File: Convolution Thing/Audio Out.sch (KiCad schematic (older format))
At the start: 25 parts, among them J4 Out Left, J5 Out Right, U4 NE5532

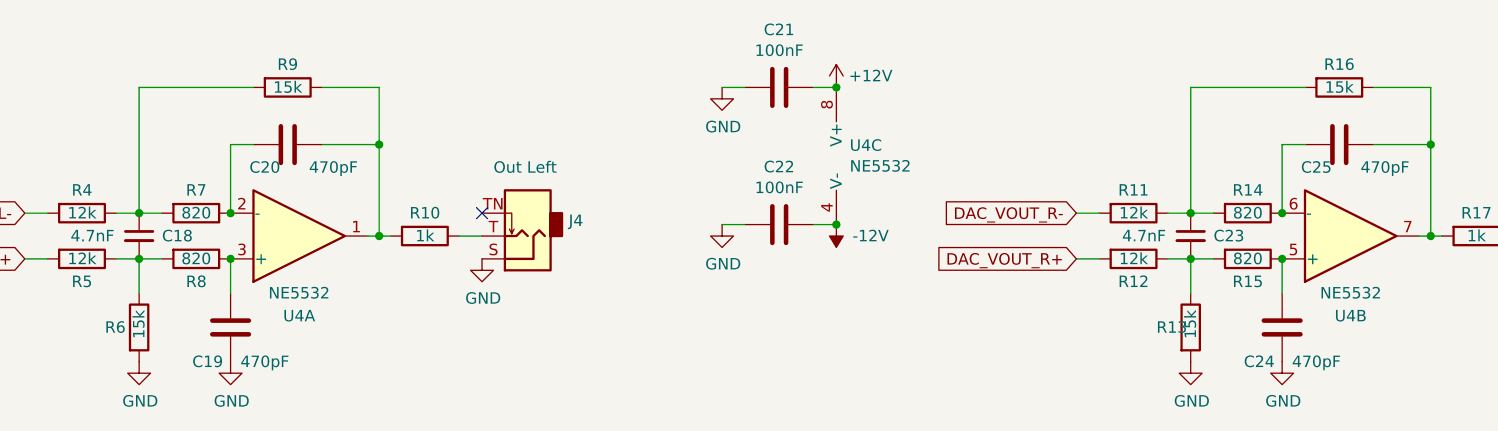
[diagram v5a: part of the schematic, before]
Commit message: Assign all footprints
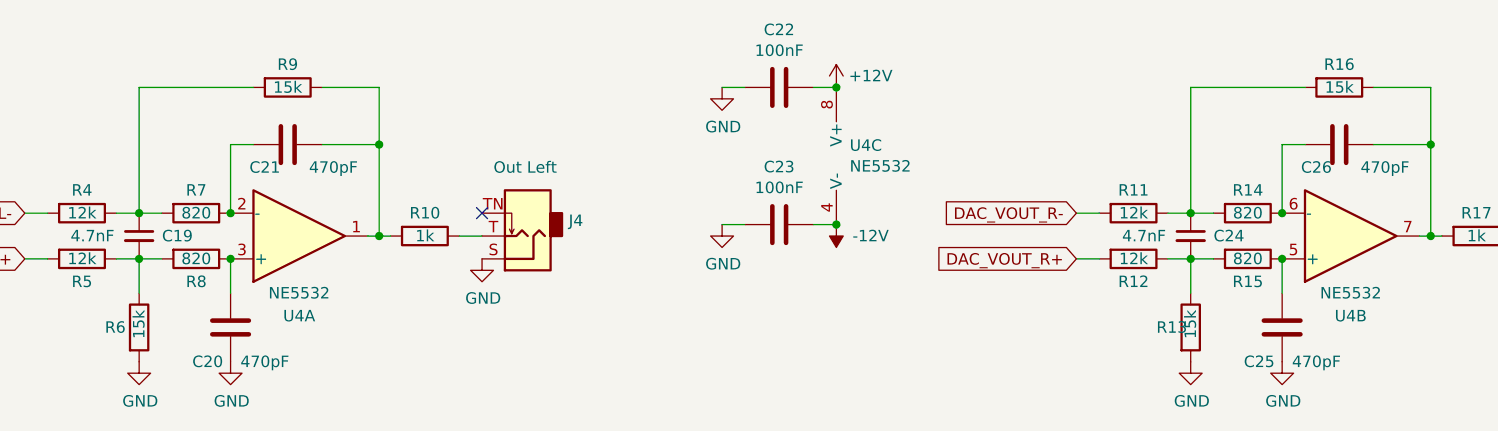
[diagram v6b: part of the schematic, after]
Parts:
- C19: renamed from C18; footprint (none) -> Capacitor_SMD:C_0805_2012Metric
- C20: renamed from C19; footprint (none) -> Capacitor_SMD:C_0805_2012Metric
- C21: renamed from C20; footprint (none) -> Capacitor_SMD:C_0805_2012Metric
- C22: renamed from C21; footprint (none) -> Capacitor_SMD:C_0805_2012Metric
- C23: renamed from C22; footprint (none) -> Capacitor_SMD:C_0805_2012Metric
- C24: renamed from C23; footprint (none) -> Capacitor_SMD:C_0805_2012Metric
- C25: renamed from C24; footprint (none) -> Capacitor_SMD:C_0805_2012Metric
- C26: renamed from C25; footprint (none) -> Capacitor_SMD:C_0805_2012Metric
- J4, J5: footprint (none) -> SamacSys:ACJMNV352S
- R10, R11, R12, R13, R14, R15, R16, R17, R4, R5, R6, R7, R8, R9: footprint (none) -> Resistor_SMD:R_0805_2012Metric
- U4: footprint (none) -> Package_SO:SOIC-8_3.9x4.9mm_P1.27mm
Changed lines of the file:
@@
 F 0 "U4" H 2350 2000 50  0000 C CNN
 F 1 "NE5532" H 2350 1900 50  0000 C CNN
-F 2 "" H 2350 1650 50  0001 C CNN
+F 2 "Package_SO:SOIC-8_3.9x4.9mm_P1.27mm" H 2350 1650 50  0001 C CNN
 F 3 "http://www.ti.com/lit/ds/symlink/ne5532.pdf" H 2350 1650 50  0001 C CNN
 	1    2350 1650
@@
 F 0 "R7" V 1800 1550 50  0000 C CNN
 F 1 "820" V 1900 1550 50  0000 C CNN
-F 2 "" V 1830 1550 50  0001 C CNN
+F 2 "Resistor_SMD:R_0805_2012Metric" V 1830 1550 50  0001 C CNN
 F 3 "~" H 1900 1550 50  0001 C CNN
 	1    1900 1550
@@
 Connection ~ 1650 1550
 $Comp
-L Device:C_Small C18
+L Device:C_Small C19
 U 1 1 611B450A
 P 1650 1650
-F 0 "C18" H 1750 1650 50  0000 L CNN
+F 0 "C19" H 1750 1650 50  0000 L CNN
 F 1 "4.7nF" H 1350 1650 50  0000 L CNN
-F 2 "" H 1650 1650 50  0001 C CNN
+F 2 "Capacitor_SMD:C_0805_2012Metric" H 1650 1650 50  0001 C CNN
 F 3 "~" H 1650 1650 50  0001 C CNN
 	1    1650 1650
@@
 F 0 "R8" V 2000 1750 50  0000 C CNN
 F 1 "820" V 1900 1750 50  0000 C CNN
-F 2 "" V 1830 1750 50  0001 C CNN
+F 2 "Resistor_SMD:R_0805_2012Metric" V 1830 1750 50  0001 C CNN
 F 3 "~" H 1900 1750 50  0001 C CNN
 	1    1900 1750
@@
 Connection ~ 1650 1750
 $Comp
-L power:GND #PWR041
+L power:GND #PWR042
 U 1 1 611B9F73
 P 1650 2200
-F 0 "#PWR041" H 1650 1950 50  0001 C CNN
+F 0 "#PWR042" H 1650 1950 50  0001 C CNN
 F 1 "GND" H 1655 2027 50  0000 C CNN
 F 2 "" H 1650 2200 50  0001 C CNN
@@
 	1650 1900 1650 1750
 $Comp
-L Device:C C19
+L Device:C C20
 U 1 1 611BBD64
 P 2050 2050
-F 0 "C19" H 2150 2200 50  0000 C CNN
+F 0 "C20" H 2150 2200 50  0000 C CNN
 F 1 "470pF" H 1900 2200 50  0000 C CNN
-F 2 "" H 2088 1900 50  0001 C CNN
+F 2 "Capacitor_SMD:C_0805_2012Metric" H 2088 1900 50  0001 C CNN
 F 3 "~" H 2050 2050 50  0001 C CNN
 	1    2050 2050
@@
 $EndComp
 $Comp
-L power:GND #PWR042
+L power:GND #PWR043
 U 1 1 611BC324
 P 2050 2200
-F 0 "#PWR042" H 2050 1950 50  0001 C CNN
+F 0 "#PWR043" H 2050 1950 50  0001 C CNN
 F 1 "GND" H 2055 2027 50  0000 C CNN
 F 2 "" H 2050 2200 50  0001 C CNN
@@
 F 0 "R10" V 2800 1650 50  0000 C CNN
 F 1 "1k" V 2900 1650 50  0000 C CNN
-F 2 "" V 2830 1650 50  0001 C CNN
+F 2 "Resistor_SMD:R_0805_2012Metric" V 2830 1650 50  0001 C CNN
 F 3 "~" H 2900 1650 50  0001 C CNN
 	1    2900 1650
@@
 	3150 1650 3050 1650
 $Comp
-L power:GND #PWR043
+L power:GND #PWR044
 U 1 1 611C0D52
 P 3150 1750
-F 0 "#PWR043" H 3150 1500 50  0001 C CNN
+F 0 "#PWR044" H 3150 1500 50  0001 C CNN
 F 1 "GND" H 3155 1577 50  0000 C CNN
 F 2 "" H 3150 1750 50  0001 C CNN
@@
 F 0 "U4" H 4758 1346 50  0000 L CNN
 F 1 "NE5532" H 4758 1255 50  0000 L CNN
-F 2 "" H 4800 1300 50  0001 C CNN
+F 2 "Package_SO:SOIC-8_3.9x4.9mm_P1.27mm" H 4800 1300 50  0001 C CNN
 F 3 "http://www.ti.com/lit/ds/symlink/ne5532.pdf" H 4800 1300 50  0001 C CNN
 	3    4800 1300
@@
 $EndComp
 $Comp
-L power:+12V #PWR046
+L power:+12V #PWR047
 U 1 1 611D5CA2
 P 4700 1000
-F 0 "#PWR046" H 4700 850 50  0001 C CNN
+F 0 "#PWR047" H 4700 850 50  0001 C CNN
 F 1 "+12V" H 4850 1050 50  0000 C CNN
 F 2 "" H 4700 1000 50  0001 C CNN
@@
 $EndComp
 $Comp
-L power:-12V #PWR047
+L power:-12V #PWR048
 U 1 1 611D5CA8
 P 4700 1600
-F 0 "#PWR047" H 4700 1700 50  0001 C CNN
+F 0 "#PWR048" H 4700 1700 50  0001 C CNN
 F 1 "-12V" H 4550 1650 50  0000 C CNN
 F 2 "" H 4700 1600 50  0001 C CNN
@@
 Connection ~ 4700 1000
 $Comp
-L Device:C C22
+L Device:C C23
 U 1 1 611D5CAF
 P 4450 1600
-F 0 "C22" V 4198 1600 50  0000 C CNN
+F 0 "C23" V 4198 1600 50  0000 C CNN
 F 1 "100nF" V 4289 1600 50  0000 C CNN
-F 2 "" H 4488 1450 50  0001 C CNN
+F 2 "Capacitor_SMD:C_0805_2012Metric" H 4488 1450 50  0001 C CNN
 F 3 "~" H 4450 1600 50  0001 C CNN
 	1    4450 1600
@@
 $EndComp
 $Comp
-L power:GND #PWR045
+L power:GND #PWR046
 U 1 1 611D5CB5
 P 4200 1600
-F 0 "#PWR045" H 4200 1350 50  0001 C CNN
+F 0 "#PWR046" H 4200 1350 50  0001 C CNN
 F 1 "GND" H 4205 1427 50  0000 C CNN
 F 2 "" H 4200 1600 50  0001 C CNN
@@
 Connection ~ 4700 1600
 $Comp
-L Device:C C21
+L Device:C C22
 U 1 1 611D5CBC
 P 4450 1000
-F 0 "C21" V 4198 1000 50  0000 C CNN
+F 0 "C22" V 4198 1000 50  0000 C CNN
 F 1 "100nF" V 4289 1000 50  0000 C CNN
-F 2 "" H 4488 850 50  0001 C CNN
+F 2 "Capacitor_SMD:C_0805_2012Metric" H 4488 850 50  0001 C CNN
 F 3 "~" H 4450 1000 50  0001 C CNN
 	1    4450 1000
@@
 $EndComp
 $Comp
-L power:GND #PWR044
+L power:GND #PWR045
 U 1 1 611D5CC2
 P 4200 1000
-F 0 "#PWR044" H 4200 750 50  0001 C CNN
+F 0 "#PWR045" H 4200 750 50  0001 C CNN
 F 1 "GND" H 4205 827 50  0000 C CNN
 F 2 "" H 4200 1000 50  0001 C CNN
@@
 F 0 "R6" H 1500 2050 50  0000 L CNN
 F 1 "15k" V 1650 2000 50  0000 L CNN
-F 2 "" V 1580 2050 50  0001 C CNN
+F 2 "Resistor_SMD:R_0805_2012Metric" V 1580 2050 50  0001 C CNN
 F 3 "~" H 1650 2050 50  0001 C CNN
 	1    1650 2050
@@
 F 0 "R5" V 1500 1750 50  0000 C CNN
 F 1 "12k" V 1400 1750 50  0000 C CNN
-F 2 "" V 1330 1750 50  0001 C CNN
+F 2 "Resistor_SMD:R_0805_2012Metric" V 1330 1750 50  0001 C CNN
 F 3 "~" H 1400 1750 50  0001 C CNN
 	1    1400 1750
@@
 F 0 "R9" V 2200 1000 50  0000 C CNN
 F 1 "15k" V 2300 1000 50  0000 C CNN
-F 2 "" V 2230 1000 50  0001 C CNN
+F 2 "Resistor_SMD:R_0805_2012Metric" V 2230 1000 50  0001 C CNN
 F 3 "~" H 2300 1000 50  0001 C CNN
 	1    2300 1000
@@
 F 0 "R4" V 1300 1550 50  0000 C CNN
 F 1 "12k" V 1400 1550 50  0000 C CNN
-F 2 "" V 1330 1550 50  0001 C CNN
+F 2 "Resistor_SMD:R_0805_2012Metric" V 1330 1550 50  0001 C CNN
 F 3 "~" H 1400 1550 50  0001 C CNN
 	1    1400 1550
@@
 	2700 1250 2700 1650
 $Comp
-L Device:C C20
+L Device:C C21
 U 1 1 611B100B
 P 2300 1250
-F 0 "C20" V 2400 1150 50  0000 C CNN
+F 0 "C21" V 2400 1150 50  0000 C CNN
 F 1 "470pF" V 2400 1450 50  0000 C CNN
-F 2 "" H 2338 1100 50  0001 C CNN
+F 2 "Capacitor_SMD:C_0805_2012Metric" H 2338 1100 50  0001 C CNN
 F 3 "~" H 2300 1250 50  0001 C CNN
 	1    2300 1250
@@
 F 0 "U4" H 6950 2000 50  0000 C CNN
 F 1 "NE5532" H 6950 1900 50  0000 C CNN
-F 2 "" H 6950 1650 50  0001 C CNN
+F 2 "Package_SO:SOIC-8_3.9x4.9mm_P1.27mm" H 6950 1650 50  0001 C CNN
 F 3 "http://www.ti.com/lit/ds/symlink/ne5532.pdf" H 6950 1650 50  0001 C CNN
 	2    6950 1650
@@
 F 0 "R14" V 6400 1550 50  0000 C CNN
 F 1 "820" V 6500 1550 50  0000 C CNN
-F 2 "" V 6430 1550 50  0001 C CNN
+F 2 "Resistor_SMD:R_0805_2012Metric" V 6430 1550 50  0001 C CNN
 F 3 "~" H 6500 1550 50  0001 C CNN
 	1    6500 1550
@@
 Connection ~ 6250 1550
 $Comp
-L Device:C_Small C23
+L Device:C_Small C24
 U 1 1 610EFD45
 P 6250 1650
-F 0 "C23" H 6350 1650 50  0000 L CNN
+F 0 "C24" H 6350 1650 50  0000 L CNN
 F 1 "4.7nF" H 5950 1650 50  0000 L CNN
-F 2 "" H 6250 1650 50  0001 C CNN
+F 2 "Capacitor_SMD:C_0805_2012Metric" H 6250 1650 50  0001 C CNN
 F 3 "~" H 6250 1650 50  0001 C CNN
 	1    6250 1650
@@
 F 0 "R15" V 6600 1750 50  0000 C CNN
 F 1 "820" V 6500 1750 50  0000 C CNN
-F 2 "" V 6430 1750 50  0001 C CNN
+F 2 "Resistor_SMD:R_0805_2012Metric" V 6430 1750 50  0001 C CNN
 F 3 "~" H 6500 1750 50  0001 C CNN
 	1    6500 1750
@@
 Connection ~ 6250 1750
 $Comp
-L power:GND #PWR048
+L power:GND #PWR049
 U 1 1 610EFD52
 P 6250 2200
-F 0 "#PWR048" H 6250 1950 50  0001 C CNN
+F 0 "#PWR049" H 6250 1950 50  0001 C CNN
 F 1 "GND" H 6255 2027 50  0000 C CNN
 F 2 "" H 6250 2200 50  0001 C CNN
@@
 	6250 1900 6250 1750
 $Comp
-L Device:C C24
+L Device:C C25
 U 1 1 610EFD59
 P 6650 2050
-F 0 "C24" H 6750 2200 50  0000 C CNN
+F 0 "C25" H 6750 2200 50  0000 C CNN
 F 1 "470pF" H 6500 2200 50  0000 C CNN
-F 2 "" H 6688 1900 50  0001 C CNN
+F 2 "Capacitor_SMD:C_0805_2012Metric" H 6688 1900 50  0001 C CNN
 F 3 "~" H 6650 2050 50  0001 C CNN
 	1    6650 2050
@@
 $EndComp
 $Comp
-L power:GND #PWR049
+L power:GND #PWR050
 U 1 1 610EFD5F
 P 6650 2200
-F 0 "#PWR049" H 6650 1950 50  0001 C CNN
+F 0 "#PWR050" H 6650 1950 50  0001 C CNN
 F 1 "GND" H 6655 2027 50  0000 C CNN
 F 2 "" H 6650 2200 50  0001 C CNN
@@
 F 0 "R17" V 7400 1650 50  0000 C CNN
 F 1 "1k" V 7500 1650 50  0000 C CNN
-F 2 "" V 7430 1650 50  0001 C CNN
+F 2 "Resistor_SMD:R_0805_2012Metric" V 7430 1650 50  0001 C CNN
 F 3 "~" H 7500 1650 50  0001 C CNN
 	1    7500 1650
@@
 	7750 1650 7650 1650
 $Comp
-L power:GND #PWR050
+L power:GND #PWR051
 U 1 1 610EFD74
 P 7750 1750
-F 0 "#PWR050" H 7750 1500 50  0001 C CNN
+F 0 "#PWR051" H 7750 1500 50  0001 C CNN
 F 1 "GND" H 7755 1577 50  0000 C CNN
 F 2 "" H 7750 1750 50  0001 C CNN
@@
 F 0 "R13" H 6100 2050 50  0000 L CNN
 F 1 "15k" V 6250 2000 50  0000 L CNN
-F 2 "" V 6180 2050 50  0001 C CNN
+F 2 "Resistor_SMD:R_0805_2012Metric" V 6180 2050 50  0001 C CNN
 F 3 "~" H 6250 2050 50  0001 C CNN
 	1    6250 2050
@@
 F 0 "R12" V 6100 1750 50  0000 C CNN
 F 1 "12k" V 6000 1750 50  0000 C CNN
-F 2 "" V 5930 1750 50  0001 C CNN
+F 2 "Resistor_SMD:R_0805_2012Metric" V 5930 1750 50  0001 C CNN
 F 3 "~" H 6000 1750 50  0001 C CNN
 	1    6000 1750
@@
 F 0 "R16" V 6800 1000 50  0000 C CNN
 F 1 "15k" V 6900 1000 50  0000 C CNN
-F 2 "" V 6830 1000 50  0001 C CNN
+F 2 "Resistor_SMD:R_0805_2012Metric" V 6830 1000 50  0001 C CNN
 F 3 "~" H 6900 1000 50  0001 C CNN
 	1    6900 1000
@@
 F 0 "R11" V 5900 1550 50  0000 C CNN
 F 1 "12k" V 6000 1550 50  0000 C CNN
-F 2 "" V 5930 1550 50  0001 C CNN
+F 2 "Resistor_SMD:R_0805_2012Metric" V 5930 1550 50  0001 C CNN
 F 3 "~" H 6000 1550 50  0001 C CNN
 	1    6000 1550
@@
 	7300 1250 7300 1650
 $Comp
-L Device:C C25
+L Device:C C26
 U 1 1 610EFDA4
 P 6900 1250
-F 0 "C25" V 7000 1150 50  0000 C CNN
+F 0 "C26" V 7000 1150 50  0000 C CNN
 F 1 "470pF" V 7000 1450 50  0000 C CNN
-F 2 "" H 6938 1100 50  0001 C CNN
+F 2 "Capacitor_SMD:C_0805_2012Metric" H 6938 1100 50  0001 C CNN
 F 3 "~" H 6900 1250 50  0001 C CNN
 	1    6900 1250
@@
 F 0 "J4" H 3171 1583 50  0000 R CNN
 F 1 "Out Left" H 3500 1350 50  0000 R CNN
-F 2 "" H 3350 1650 50  0001 C CNN
+F 2 "SamacSys:ACJMNV352S" H 3350 1650 50  0001 C CNN
 F 3 "~" H 3350 1650 50  0001 C CNN
 	1    3350 1650
@@
 F 0 "J5" H 7771 1583 50  0000 R CNN
 F 1 "Out Right" H 8100 1350 50  0000 R CNN
-F 2 "" H 7950 1650 50  0001 C CNN
+F 2 "SamacSys:ACJMNV352S" H 7950 1650 50  0001 C CNN
 F 3 "~" H 7950 1650 50  0001 C CNN
 	1    7950 1650

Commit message: PCB layout work and related changes to the schematic
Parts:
- J3: renamed from J4; footprint SamacSys:ACJMNV352S -> Connector_Audio:Jack_3.5mm_QingPu_WQP-PJ398SM_Vertical_CircularHoles
- J4: renamed from J5; footprint SamacSys:ACJMNV352S -> Connector_Audio:Jack_3.5mm_QingPu_WQP-PJ398SM_Vertical_CircularHoles
- renumbered C19 to C15, C20 to C16, C21 to C17, C22 to C18, C23 to C19, C24 to C20, C25 to C21, C26 to C22, R12 to R10, R13 to R11, R14 to R12, R15 to R13, R16 to R14, R17 to R15, R4 to R2, R5 to R3, R6 to R4, R7 to R5, R8 to R6, R9 to R7, R10 to R8, R11 to R9, U4 to U3
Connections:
- net DAC_VOUT_L+ renamed CODEC_VOUT_L+
- net DAC_VOUT_L- renamed CODEC_VOUT_L-
- net DAC_VOUT_R+ renamed CODEC_VOUT_R+
- net DAC_VOUT_R- renamed CODEC_VOUT_R-
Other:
- moved on the sheet: C15, C16, C17, C20, C21, C22, J3, J4, R10, R11, R12, R13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
